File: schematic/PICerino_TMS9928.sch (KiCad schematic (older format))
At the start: 45 parts, among them CON1 PICERINO-EDGE, J1 Conn_01x02, J2 Conn_01x02, J3 Conn_01x02, J4 Conn_01x02, Y1 Crystal

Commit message: added 470 ohm load resistors to output of VDP pre TI spec (whoops)
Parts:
- added R7, R8, R9: 470R, Resistor_THT:R_Axial_DIN0207_L6.3mm_D2.5mm_P7.62mm_Horizontal, symbol Device:R
- J2: value Conn_01x02 -> Y_Conn_01x02
- J3: value Conn_01x02 -> BY_Conn_01x02
- J4: value Conn_01x02 -> RY_Conn_01x02
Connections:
- net VSS: now also R7.2, R8.1, R9.2
- net Y: now also R7.1
- net Yb: now also R9.1
- net Yr: now also R8.2
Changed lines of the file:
@@
 P 6000 7450
 F 0 "J2" H 6080 7442 50  0000 L CNN
-F 1 "Conn_01x02" H 6080 7351 50  0000 L CNN
+F 1 "Y_Conn_01x02" H 6080 7351 50  0000 L CNN
 F 2 "Connector_PinHeader_2.54mm:PinHeader_1x02_P2.54mm_Vertical" H 6000 7450 50  0001 C CNN
 F 3 "~" H 6000 7450 50  0001 C CNN
@@
 P 9200 7350
 F 0 "J4" H 9280 7342 50  0000 L CNN
-F 1 "Conn_01x02" H 9280 7251 50  0000 L CNN
+F 1 "RY_Conn_01x02" H 9280 7251 50  0000 L CNN
 F 2 "Connector_PinHeader_2.54mm:PinHeader_1x02_P2.54mm_Vertical" H 9200 7350 50  0001 C CNN
 F 3 "~" H 9200 7350 50  0001 C CNN
@@
 P 10350 7450
 F 0 "J3" H 10430 7442 50  0000 L CNN
-F 1 "Conn_01x02" H 10430 7351 50  0000 L CNN
+F 1 "BY_Conn_01x02" H 10430 7351 50  0000 L CNN
 F 2 "Connector_PinHeader_2.54mm:PinHeader_1x02_P2.54mm_Vertical" H 10350 7450 50  0001 C CNN
 F 3 "~" H 10350 7450 50  0001 C CNN
@@
 	6250 7150 6650 7150
 Wire Wire Line
-	6250 5650 6250 7150
+	6250 5650 6250 6300
 Wire Wire Line
 	6350 5550 6350 6650
 Wire Wire Line
-	8600 6650 6350 6650
-Wire Wire Line
 	6450 5450 6450 6550
 Wire Wire Line
-	6450 6550 9750 6550
+	6450 6550 8850 6550
 Wire Wire Line
 	9750 6550 9750 7150
@@
 Wire Bus Line
 	3500 3550 3500 4250
+$Comp
+L Device:R R7
+U 1 1 621E3E74
+P 6100 6300
+F 0 "R7" H 6170 6346 50  0000 L CNN
+F 1 "470R" H 6170 6255 50  0000 L CNN
+F 2 "Resistor_THT:R_Axial_DIN0207_L6.3mm_D2.5mm_P7.62mm_Horizontal" V 6030 6300 50  0001 C CNN
+F 3 "~" H 6100 6300 50  0001 C CNN
+	1    6100 6300
+	0    1    1    0
+$EndComp
+Connection ~ 6250 6300
+Wire Wire Line
+	6250 6300 6250 7150
+$Comp
+L Device:R R9
+U 1 1 621E4A45
+P 8850 6700
+F 0 "R9" H 8920 6746 50  0000 L CNN
+F 1 "470R" H 8920 6655 50  0000 L CNN
+F 2 "Resistor_THT:R_Axial_DIN0207_L6.3mm_D2.5mm_P7.62mm_Horizontal" V 8780 6700 50  0001 C CNN
+F 3 "~" H 8850 6700 50  0001 C CNN
+	1    8850 6700
+	1    0    0    -1
+$EndComp
+Connection ~ 8850 6550
+Wire Wire Line
+	8850 6550 9750 6550
+$Comp
+L Device:R R8
+U 1 1 621E5A63
+P 6550 6800
+F 0 "R8" H 6620 6846 50  0000 L CNN
+F 1 "470R" H 6620 6755 50  0000 L CNN
+F 2 "Resistor_THT:R_Axial_DIN0207_L6.3mm_D2.5mm_P7.62mm_Horizontal" V 6480 6800 50  0001 C CNN
+F 3 "~" H 6550 6800 50  0001 C CNN
+	1    6550 6800
+	-1   0    0    1
+$EndComp
+$Comp
+L power:VSS #PWR0145
+U 1 1 621E625A
+P 6550 6950
+F 0 "#PWR0145" H 6550 6800 50  0001 C CNN
+F 1 "VSS" H 6450 7050 50  0000 C CNN
+F 2 "" H 6550 6950 50  0001 C CNN
+F 3 "" H 6550 6950 50  0001 C CNN
+	1    6550 6950
+	-1   0    0    1
+$EndComp
+$Comp
+L power:VSS #PWR0146
+U 1 1 621E6A5C
+P 8850 6850
+F 0 "#PWR0146" H 8850 6700 50  0001 C CNN
+F 1 "VSS" H 8750 6950 50  0000 C CNN
+F 2 "" H 8850 6850 50  0001 C CNN
+F 3 "" H 8850 6850 50  0001 C CNN
+	1    8850 6850
+	-1   0    0    1
+$EndComp
+$Comp
+L power:VSS #PWR0147
+U 1 1 621E73D1
+P 5950 6300
+F 0 "#PWR0147" H 5950 6150 50  0001 C CNN
+F 1 "VSS" H 5850 6400 50  0000 C CNN
+F 2 "" H 5950 6300 50  0001 C CNN
+F 3 "" H 5950 6300 50  0001 C CNN
+	1    5950 6300
+	0    -1   -1   0
+$EndComp
+Connection ~ 6550 6650
+Wire Wire Line
+	6550 6650 8600 6650
+Wire Wire Line
+	6350 6650 6550 6650
 $EndSCHEMATC

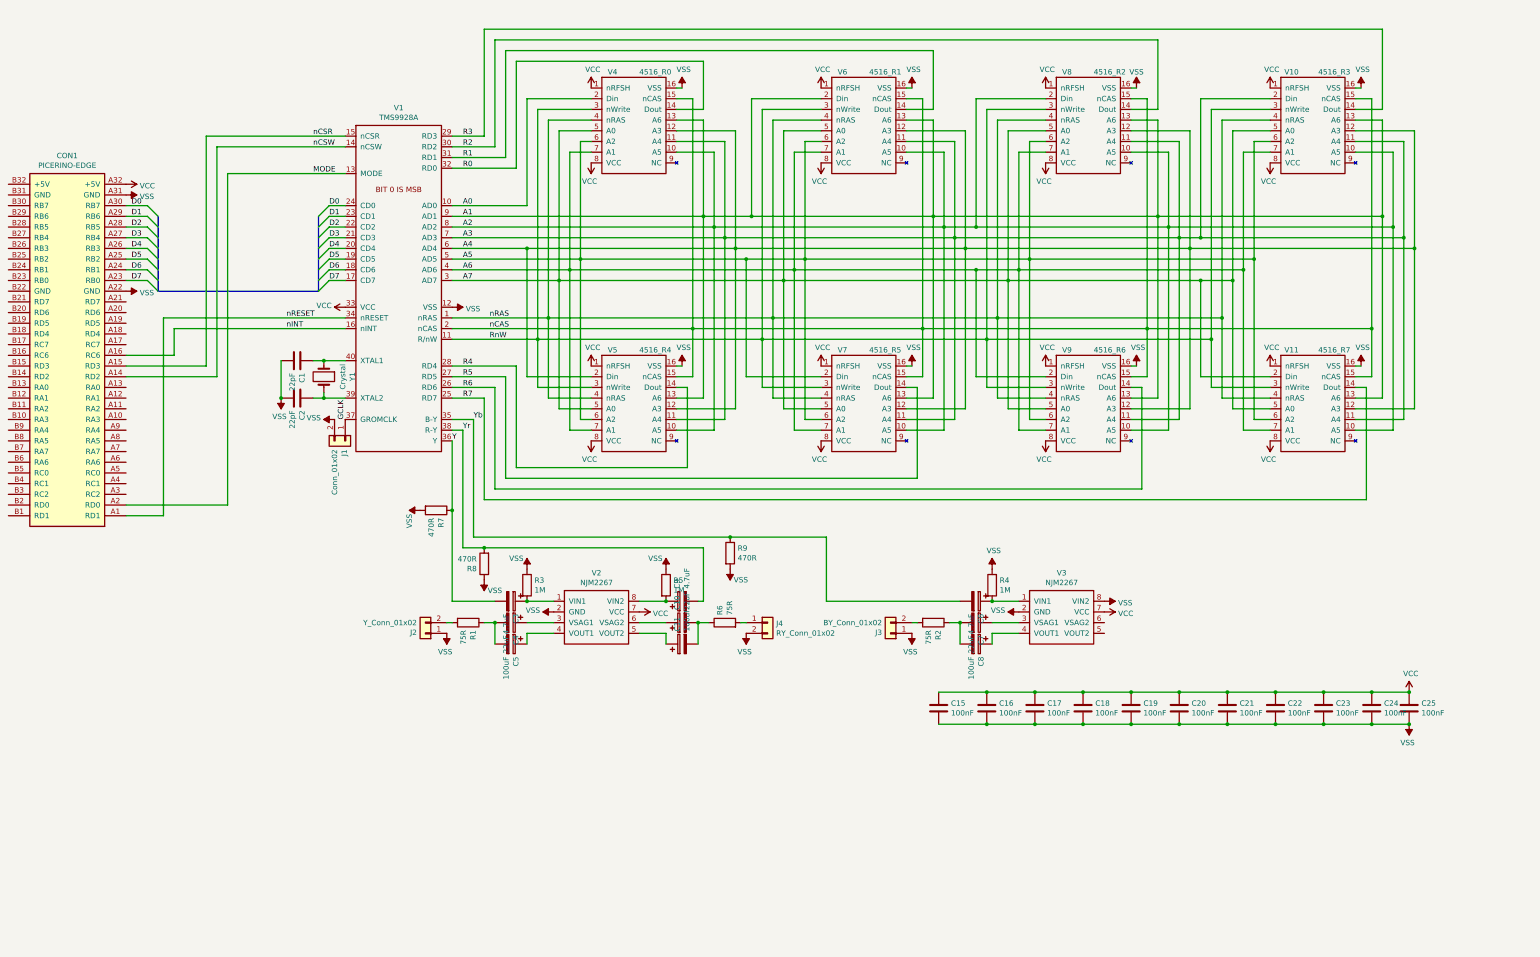
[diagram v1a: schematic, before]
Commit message: updated schematic with new features. 1) test points for dram testing. 2) jumpers to route video output signals for testing.
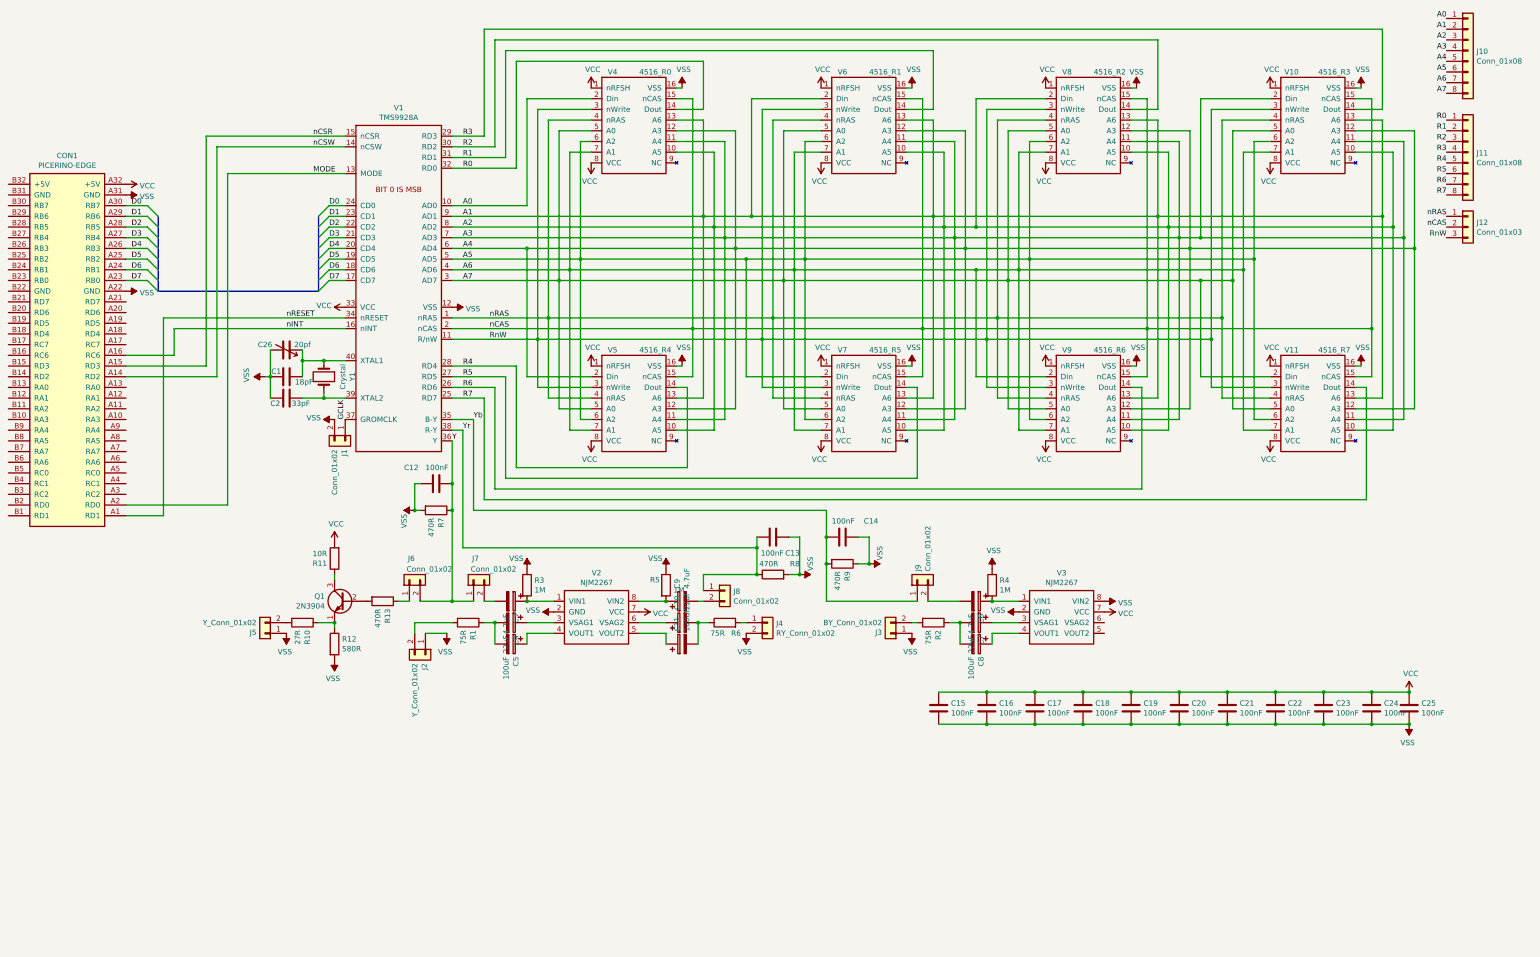
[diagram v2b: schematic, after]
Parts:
- added C12, C13, C14: 100nF, Capacitor_THT:C_Disc_D4.7mm_W2.5mm_P5.00mm, symbol Device:C
- added C26: 20pf, Capacitor_THT:C_Rect_L10.0mm_W5.0mm_P5.00mm_P7.50mm, symbol Device:C_Variable
- added J10, J11: Conn_01x08, Connector_PinHeader_2.54mm:PinHeader_1x08_P2.54mm_Vertical, symbol Connector_Generic:Conn_01x08
- added J12: Conn_01x03, Connector_PinHeader_2.54mm:PinHeader_1x03_P2.54mm_Vertical, symbol Connector_Generic:Conn_01x03
- added J5: Y_Conn_01x02, Connector_PinHeader_2.54mm:PinHeader_1x02_P2.54mm_Vertical, symbol Connector_Generic:Conn_01x02
- added J6, J7, J8, J9: Conn_01x02, Connector_PinHeader_2.54mm:PinHeader_1x02_P2.54mm_Vertical, symbol Connector_Generic:Conn_01x02
- added Q1: 2N3904, Package_TO_SOT_THT:TO-92_Wide, symbol Transistor_BJT:2N3904
- added R10: 27R, Resistor_THT:R_Axial_DIN0207_L6.3mm_D2.5mm_P7.62mm_Horizontal, symbol Device:R
- added R11: 10R, Resistor_THT:R_Axial_DIN0207_L6.3mm_D2.5mm_P7.62mm_Horizontal, symbol Device:R
- added R12: 580R, Resistor_THT:R_Axial_DIN0207_L6.3mm_D2.5mm_P7.62mm_Horizontal, symbol Device:R
- added R13: 470R, Resistor_THT:R_Axial_DIN0207_L6.3mm_D2.5mm_P7.62mm_Horizontal, symbol Device:R
- C1: value 22pF -> 18pF
- C2: value 22pF -> 33pF
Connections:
- net A0: now also J10.1 (Pin_1)
- net A1: now also J10.2 (Pin_2)
- net A2: now also J10.3 (Pin_3)
- net A3: now also J10.4 (Pin_4)
- net A4: now also J10.5 (Pin_5)
- net A5: now also J10.6 (Pin_6)
- net A6: now also J10.7 (Pin_7)
- net A7: now also J10.8 (Pin_8)
- net R0: now also J11.1 (Pin_1)
- net R1: now also J11.2 (Pin_2)
- net R2: now also J11.3 (Pin_3)
- net R3: now also J11.4 (Pin_4)
- net R4: now also J11.5 (Pin_5)
- net R5: now also J11.6 (Pin_6)
- net R6: now also J11.7 (Pin_7)
- net R7: now also J11.8 (Pin_8)
- net RnW: now also J12.3 (Pin_3)
- net VCC: now also R11.2
- net VSS: now also C1.1, R8.2, R9.1, C12.2, C13.2, C14.1, C26.2, J5.1 (Pin_1), R12.2; no longer C1.2, R8.1, R9.2
- net Y: now also C12.1, J6.2 (Pin_2), J7.1 (Pin_1); no longer C3.2
- net Yb: now also R9.2, C14.2, J9.1 (Pin_1); no longer C6.2, R9.1
- net Yr: now also R8.1, C13.1, J8.1 (Pin_1); no longer C9.2, R8.2
- net nCAS: now also J12.2 (Pin_2)
- net nRAS: now also J12.1 (Pin_1)
- net at V1.40 (XTAL1), Y1.1: now also C1.2, C26.1; no longer C1.1
- new net: C3.2, J7.2 (Pin_2)
- new net: C6.2, J9.2 (Pin_2)
- new net: J6.1 (Pin_1), R13.1
- new net: Q1.2 (B), R13.2
- new net: Q1.1 (E), R10.1, R12.1
- new net: J5.2 (Pin_2), R10.2
- new net: Q1.3 (C), R11.1
- new net: C9.2, J8.2 (Pin_2)
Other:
- moved on the sheet: C1, C2, J2, R8, R9

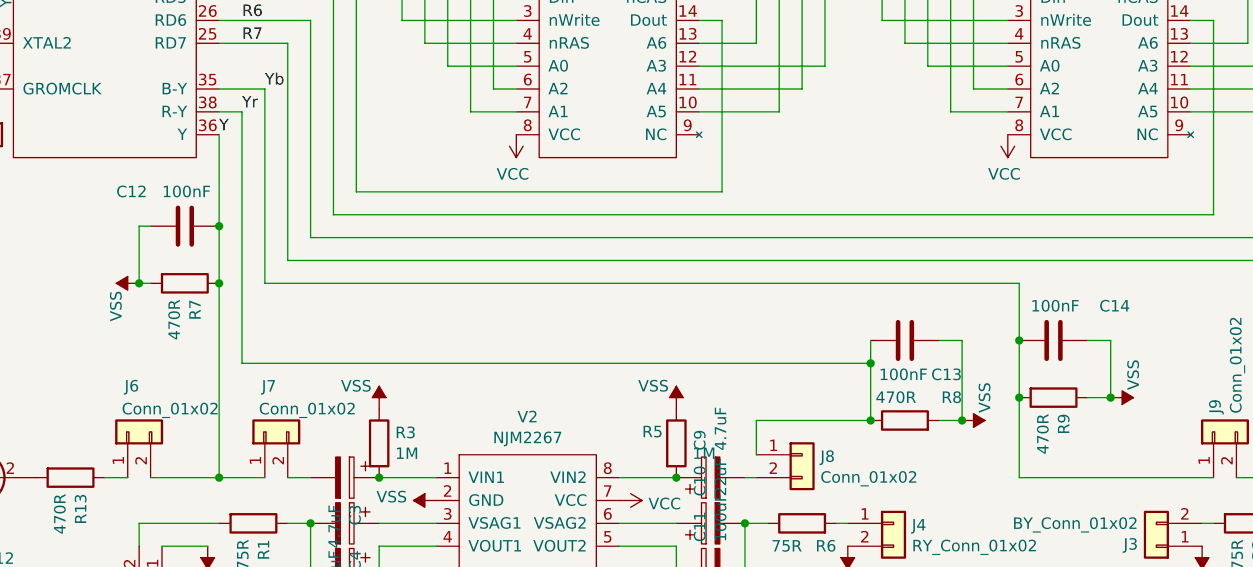
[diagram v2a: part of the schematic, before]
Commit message: schematic fix, 100nF cap is way too high a value and filters and the backporch of the signal (blurs it). 220pF is the value from a few TI example schematics. Works great, clear picture
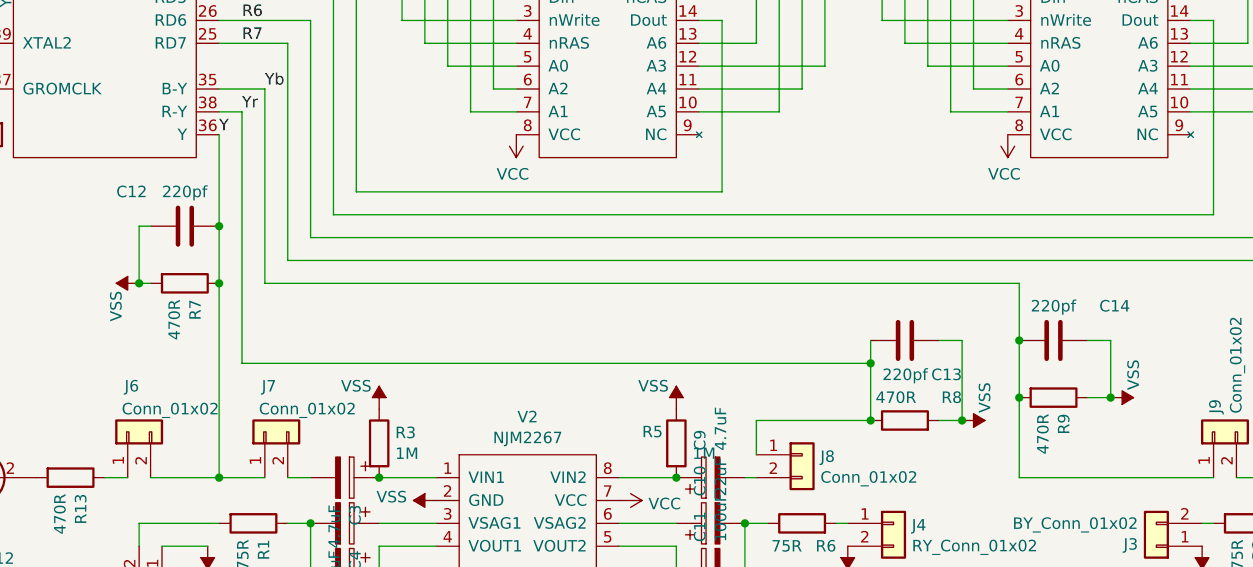
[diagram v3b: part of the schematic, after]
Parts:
- C12, C13, C14: value 100nF -> 220pf
- J10, J11: footprint Connector_PinHeader_2.54mm:PinHeader_1x08_P2.54mm_Vertical -> Package_SIP:SIP-8_19x3mm_P2.54mm
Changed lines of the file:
@@
 P 6100 6050
 F 0 "C12" V 5950 5750 50  0000 L CNN
-F 1 "100nF" V 5950 5950 50  0000 L CNN
+F 1 "220pf" V 5950 5950 50  0000 L CNN
 F 2 "Capacitor_THT:C_Disc_D4.7mm_W2.5mm_P5.00mm" H 6138 5900 50  0001 C CNN
 F 3 "~" H 6100 6050 50  0001 C CNN
@@
 P 9900 6550
 F 0 "C14" V 9750 6750 50  0000 L CNN
-F 1 "100nF" V 9750 6450 50  0000 L CNN
+F 1 "220pf" V 9750 6450 50  0000 L CNN
 F 2 "Capacitor_THT:C_Disc_D4.7mm_W2.5mm_P5.00mm" H 9938 6400 50  0001 C CNN
 F 3 "~" H 9900 6550 50  0001 C CNN
@@
 P 9250 6550
 F 0 "C13" V 9100 6300 50  0000 L CNN
-F 1 "100nF" V 9100 6450 50  0000 L CNN
+F 1 "220pf" V 9100 6450 50  0000 L CNN
 F 2 "Capacitor_THT:C_Disc_D4.7mm_W2.5mm_P5.00mm" H 9288 6400 50  0001 C CNN
 F 3 "~" H 9250 6550 50  0001 C CNN
@@
 F 0 "J10" H 15830 1992 50  0000 L CNN
 F 1 "Conn_01x08" H 15830 1901 50  0000 L CNN
-F 2 "Connector_PinHeader_2.54mm:PinHeader_1x08_P2.54mm_Vertical" H 15750 2000 50  0001 C CNN
+F 2 "Package_SIP:SIP-8_19x3mm_P2.54mm" H 15750 2000 50  0001 C CNN
 F 3 "~" H 15750 2000 50  0001 C CNN
 	1    15750 2000
@@
 F 0 "J11" H 15830 2942 50  0000 L CNN
 F 1 "Conn_01x08" H 15830 2851 50  0000 L CNN
-F 2 "Connector_PinHeader_2.54mm:PinHeader_1x08_P2.54mm_Vertical" H 15750 2950 50  0001 C CNN
+F 2 "Package_SIP:SIP-8_19x3mm_P2.54mm" H 15750 2950 50  0001 C CNN
 F 3 "~" H 15750 2950 50  0001 C CNN
 	1    15750 2950
@@
 Wire Wire Line
 	6250 6300 6250 7150
+Connection ~ 6250 7150
+Wire Wire Line
+	6250 7150 6450 7150
 Wire Bus Line
 	5000 3550 5000 4250
 Wire Bus Line
 	3500 3550 3500 4250
-Connection ~ 6250 7150
-Wire Wire Line
-	6250 7150 6450 7150
 $EndSCHEMATC
